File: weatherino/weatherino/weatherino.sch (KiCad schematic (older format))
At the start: 11 parts, among them U1 TP4056_BD, U2 BMP280_BD, U3 SHT31_BD, U4 Moteino_hcw

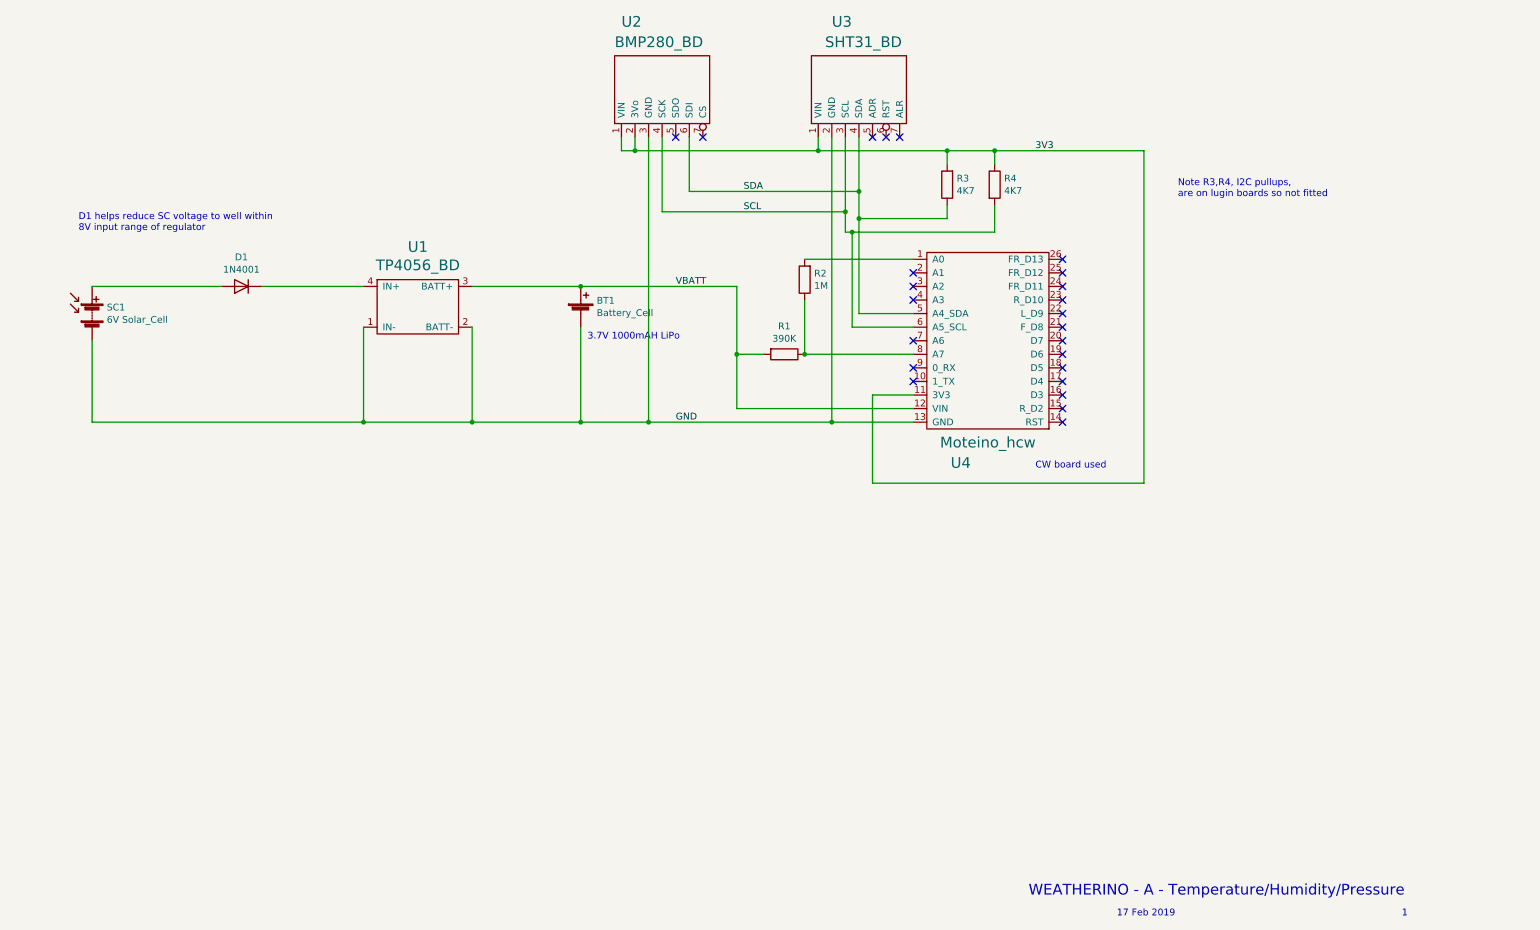
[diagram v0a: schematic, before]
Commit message: update schematic
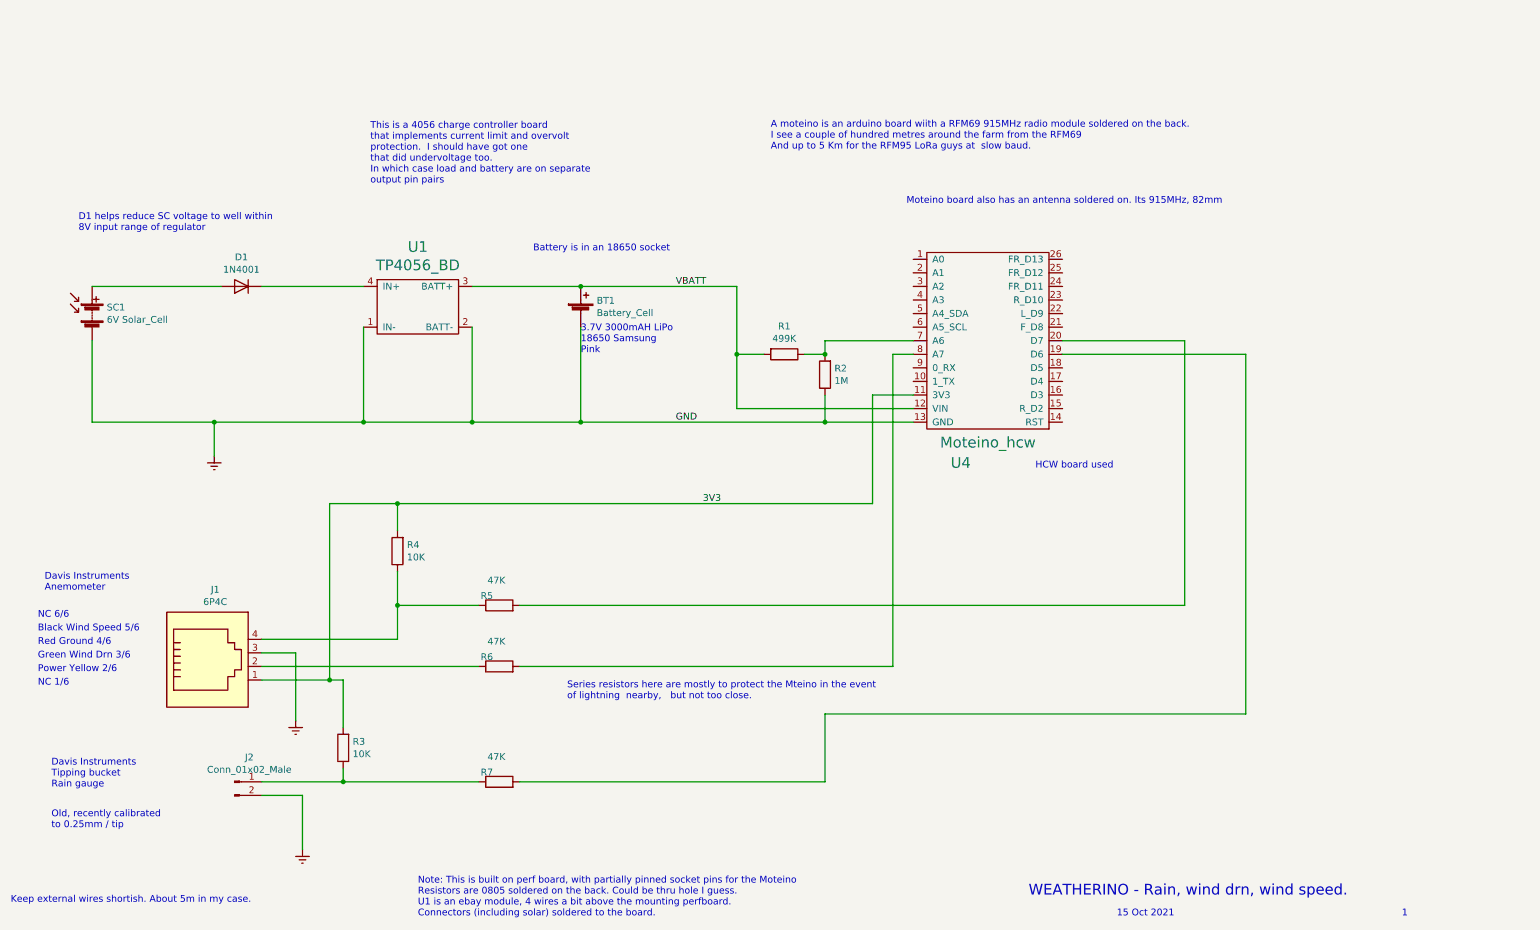
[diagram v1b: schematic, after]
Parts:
- removed U2: BMP280_BD, symbol swinggate_sch:BMP280_BD
- removed U3: SHT31_BD, symbol swinggate_sch:SHT31_BD
- added J1: 6P4C, symbol Connector:6P4C
- added J2: Conn_01x02_Male, symbol Connector:Conn_01x02_Male
- added R4: 10K, symbol Device:R
- added R5, R7: 47K, symbol Device:R
- R1: value 390K -> 499K
- R3: value 4K7 -> 10K
- R6: renamed from R4; value 4K7 -> 47K
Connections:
- net 3V3: now also J1.1, R4.2; no longer R6.1
- net at U4.1 (A0): no longer R2.2
- net at U4.19 (D6): now also R7.2
- net at U4.20 (D7): now also R5.2
- net at U4.7 (A6): now also R1.1, R2.2
- net GND renamed Earth
- net Earth: now also R2.1, J1.3, J2.2 (Pin_2)
- net SCL: no longer names the net of U4.6 (A5_SCL)
- net SCL: no longer R6.2
- net SDA: no longer names the net of U4.5 (A4_SDA)
- net SDA: no longer R3.1
- new net: R6.2, U4.8 (A7)
- new net: J1.2, R6.1
- new net: J2.1 (Pin_1), R3.1, R7.1
- new net: J1.4, R4.1, R5.1
- no-connect marks 24 -> 0
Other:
- note added: "15 Oct 2021"
- note added: "3.7V 3000mAH LiPo \n18650 Samsung\nPink"
- note added: "A moteino is an arduino board wiith a RFM69 915MHz radio module soldered on the back. \nI see a couple of hundred metres around the farm from the RFM69\nAnd up to 5 Km for the RFM95 LoRa guys at slow baud."
- note added: "Battery is in an 18650 socket"
- note added: "Black Wind Speed 5/6"
- note added: "Davis Instruments \nTipping bucket\nRain gauge"
- note added: "Davis Instruments\nAnemometer"
- note added: "Green Wind Drn 3/6"
- note added: "HCW board used"
- note added: "Keep external wires shortish. About 5m in my case."
- note added: "Moteino board also has an antenna soldered on. Its 915MHz, 82mm"
- note added: "NC 1/6"
- note added: "NC 6/6"
- note added: "Note: This is built on perf board, with partially pinned socket pins for the Moteino\nResistors are 0805 soldered on the back. Could be thru hole I guess.\nU1 is an ebay module, 4 wires a bit above the mounting perfboard.\nConnectors (including solar) soldered to the board."
- note added: "Old, recently calibrated\nto 0.25mm / tip"
- note added: "Power Yellow 2/6"
- note added: "Red Ground 4/6"
- note added: "Series resistors here are mostly to protect the Mteino in the event \nof lightning nearby, but not too close."
- note added: "This is a 4056 charge controller board\nthat implements current limit and overvolt \nprotection. I should have got one \nthat did undervoltage too. \nIn which case load and battery are on separate \noutput pin pairs"
- note added: "WEATHERINO - Rain, wind drn, wind speed."
- note removed: "17 Feb 2019"
- note removed: "3.7V 1000mAH LiPo"
- note removed: "CW board used"
- note removed: "Note R3,R4, I2C pullups,\nare on lugin boards so not fitted"
- note removed: "WEATHERINO - A - Temperature/Humidity/Pressure"
- moved on the sheet: R2, R6

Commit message: address emi susceptibility and contact bounce on rain.
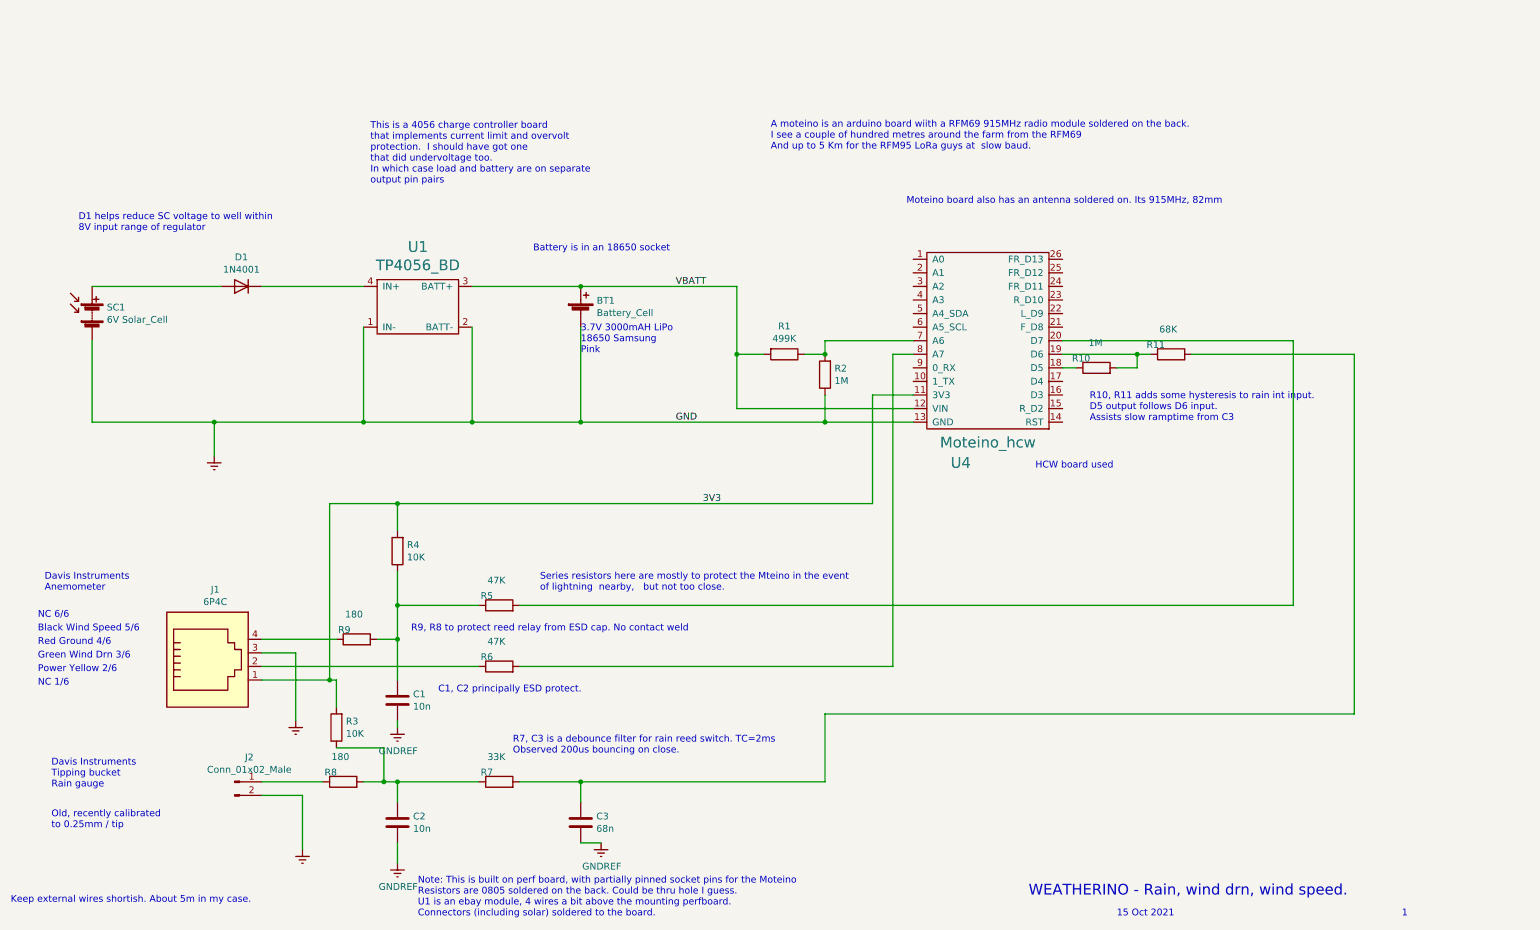
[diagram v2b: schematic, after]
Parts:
- added C1, C2: 10n, symbol Device:C
- added C3: 68n, symbol Device:C
- added R10: 1M, symbol Device:R
- added R11: 68K, symbol Device:R
- added R8, R9: 180, symbol Device:R
- R7: value 47K -> 33K
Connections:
- net at U4.18 (D5): now also R10.1
- net at U4.19 (D6): now also R10.2, R11.1; no longer R7.2
- net at R3.1, R7.1: now also C2.1, R8.2; no longer J2.1 (Pin_1)
- net at R4.1, R5.1: now also C1.1, R9.2; no longer J1.4
- new net: J2.1 (Pin_1), R8.1
- new net: J1.4, R9.1
- new net: C3.1, R11.2, R7.2
- new net GNDREF: C1.2, C2.2, C3.2
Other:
- note added: "C1, C2 principally ESD protect."
- note added: "R10, R11 adds some hysteresis to rain int input. \nD5 output follows D6 input. \nAssists slow ramptime from C3"
- note added: "R7, C3 is a debounce filter for rain reed switch. TC=2ms\nObserved 200us bouncing on close."
- note added: "R9, R8 to protect reed relay from ESD cap. No contact weld"
- moved on the sheet: R3
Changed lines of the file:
@@
 L Device:R R3
 U 1 1 616CDA02
-P 2950 6400
-F 0 "R3" H 2880 6354 50  0000 R CNN
-F 1 "10K" H 2880 6445 50  0000 R CNN
-F 2 "" V 2880 6400 50  0001 C CNN
-F 3 "~" H 2950 6400 50  0001 C CNN
-	1    2950 6400
+P 2900 6250
+F 0 "R3" H 2830 6204 50  0000 R CNN
+F 1 "10K" H 2830 6295 50  0000 R CNN
+F 2 "" V 2830 6250 50  0001 C CNN
+F 3 "~" H 2900 6250 50  0001 C CNN
+	1    2900 6250
 	-1   0    0    1
 $EndComp
-Wire Wire Line
-	2950 6550 2950 6650
 $Comp
 L Device:R R7
@@
 P 4100 6650
 F 0 "R7" V 4170 6696 50  0000 L CNN
-F 1 "47K" V 4284 6605 50  0000 L CNN
+F 1 "33K" V 4284 6605 50  0000 L CNN
 F 2 "" V 4030 6650 50  0001 C CNN
 F 3 "~" H 4100 6650 50  0001 C CNN
@@
 $EndComp
 Wire Wire Line
-	2950 6250 2950 5900
-Wire Wire Line
-	2950 5900 2850 5900
-Connection ~ 2850 5900
-Wire Wire Line
 	3350 4800 3350 4600
 Connection ~ 3350 4600
@@
 	3350 5100 3350 5350
 Wire Wire Line
-	2350 5600 3350 5600
-Wire Wire Line
 	3350 5600 3350 5350
 Connection ~ 3350 5350
 Wire Wire Line
 	2350 5800 3950 5800
-Wire Wire Line
-	2350 6650 2950 6650
-Wire Wire Line
-	2950 6650 3950 6650
-Connection ~ 2950 6650
 Wire Wire Line
 	6850 3800 6850 4600
@@
 $EndComp
 Wire Wire Line
-	4250 5350 9150 5350
-Wire Wire Line
 	7150 3400 6500 3400
 Wire Wire Line
@@
 	6500 6650 6500 6150
 Wire Wire Line
-	6500 6150 9600 6150
-Wire Wire Line
-	9600 6150 9600 3500
-Wire Wire Line
-	4250 6650 6500 6650
-Wire Wire Line
-	8250 3500 9600 3500
-Wire Wire Line
-	8250 3400 9150 3400
-Wire Wire Line
-	9150 3400 9150 5350
+	10400 6150 10400 3500
+Wire Wire Line
+	4250 6650 4700 6650
+Wire Wire Line
+	9950 3400 9950 5350
 Wire Wire Line
 	7000 3500 7000 5800
@@
 Text Notes 3500 7650 0    50   ~ 0
 Note: This is built on perf board, with partially pinned socket pins for the Moteino\nResistors are 0805 soldered on the back. Could be thru hole I guess.\nU1 is an ebay module, 4 wires a bit above the mounting perfboard.\nConnectors (including solar) soldered to the board.
-Text Notes 4600 6050 0    50   ~ 0
+Text Notes 4400 5250 0    50   ~ 0
 Series resistors here are mostly to protect the Mteino in the event \nof lightning  nearby,   but not too close.
 Text Notes 500  7550 0    50   ~ 0
@@
 Text Notes 6100 2000 0    50   ~ 0
 A moteino is an arduino board wiith a RFM69 915MHz radio module soldered on the back.  \nI see a couple of hundred metres around the farm from the RFM69\nAnd up to 5 Km for the RFM95 LoRa guys at  slow baud.
+$Comp
+L Device:R R10
+U 1 1 6175B278
+P 8500 3600
+F 0 "R10" V 8570 3646 50  0000 L CNN
+F 1 "1M" V 8684 3555 50  0000 L CNN
+F 2 "" V 8430 3600 50  0001 C CNN
+F 3 "~" H 8500 3600 50  0001 C CNN
+	1    8500 3600
+	0    -1   -1   0
+$EndComp
+$Comp
+L Device:R R11
+U 1 1 6175C380
+P 9050 3500
+F 0 "R11" V 9120 3546 50  0000 L CNN
+F 1 "68K" V 9234 3455 50  0000 L CNN
+F 2 "" V 8980 3500 50  0001 C CNN
+F 3 "~" H 9050 3500 50  0001 C CNN
+	1    9050 3500
+	0    -1   -1   0
+$EndComp
+Wire Wire Line
+	8250 3600 8350 3600
+Wire Wire Line
+	8250 3500 8800 3500
+Wire Wire Line
+	8650 3600 8800 3600
+Wire Wire Line
+	8800 3600 8800 3500
+Connection ~ 8800 3500
+Wire Wire Line
+	8800 3500 8900 3500
+Wire Wire Line
+	8250 3400 9950 3400
+Wire Wire Line
+	4250 5350 9950 5350
+Wire Wire Line
+	9200 3500 10400 3500
+Wire Wire Line
+	6500 6150 10400 6150
+$Comp
+L Device:R R8
+U 1 1 61783C0D
+P 2950 6650
+F 0 "R8" V 3020 6696 50  0000 L CNN
+F 1 "180" V 3134 6605 50  0000 L CNN
+F 2 "" V 2880 6650 50  0001 C CNN
+F 3 "~" H 2950 6650 50  0001 C CNN
+	1    2950 6650
+	0    -1   -1   0
+$EndComp
+$Comp
+L Device:C C2
+U 1 1 61785064
+P 3350 6950
+F 0 "C2" H 3465 6996 50  0000 L CNN
+F 1 "10n" H 3465 6905 50  0000 L CNN
+F 2 "" H 3388 6800 50  0001 C CNN
+F 3 "~" H 3350 6950 50  0001 C CNN
+	1    3350 6950
+	1    0    0    -1
+$EndComp
+$Comp
+L Device:C C3
+U 1 1 61785E2B
+P 4700 6950
+F 0 "C3" H 4815 6996 50  0000 L CNN
+F 1 "68n" H 4815 6905 50  0000 L CNN
+F 2 "" H 4738 6800 50  0001 C CNN
+F 3 "~" H 4700 6950 50  0001 C CNN
+	1    4700 6950
+	1    0    0    -1
+$EndComp
+$Comp
+L Device:C C1
+U 1 1 6178DBD0
+P 3350 6050
+F 0 "C1" H 3465 6096 50  0000 L CNN
+F 1 "10n" H 3465 6005 50  0000 L CNN
+F 2 "" H 3388 5900 50  0001 C CNN
+F 3 "~" H 3350 6050 50  0001 C CNN
+	1    3350 6050
+	1    0    0    -1
+$EndComp
+$Comp
+L Device:R R9
+U 1 1 6178FA99
+P 3050 5600
+F 0 "R9" V 3120 5646 50  0000 L CNN
+F 1 "180" V 3234 5555 50  0000 L CNN
+F 2 "" V 2980 5600 50  0001 C CNN
+F 3 "~" H 3050 5600 50  0001 C CNN
+	1    3050 5600
+	0    -1   -1   0
+$EndComp
+$Comp
+L power:GNDREF #PWR02
+U 1 1 617934F1
+P 3350 7250
+F 0 "#PWR02" H 3350 7000 50  0001 C CNN
+F 1 "GNDREF" H 3355 7077 50  0000 C CNN
+F 2 "" H 3350 7250 50  0001 C CNN
+F 3 "" H 3350 7250 50  0001 C CNN
+	1    3350 7250
+	1    0    0    -1
+$EndComp
+$Comp
+L power:GNDREF #PWR03
+U 1 1 617940BA
+P 4850 7100
+F 0 "#PWR03" H 4850 6850 50  0001 C CNN
+F 1 "GNDREF" H 4855 6927 50  0000 C CNN
+F 2 "" H 4850 7100 50  0001 C CNN
+F 3 "" H 4850 7100 50  0001 C CNN
+	1    4850 7100
+	1    0    0    -1
+$EndComp
+$Comp
+L power:GNDREF #PWR01
+U 1 1 61794C63
+P 3350 6250
+F 0 "#PWR01" H 3350 6000 50  0001 C CNN
+F 1 "GNDREF" H 3355 6077 50  0000 C CNN
+F 2 "" H 3350 6250 50  0001 C CNN
+F 3 "" H 3350 6250 50  0001 C CNN
+	1    3350 6250
+	1    0    0    -1
+$EndComp
+Wire Wire Line
+	2350 5600 2900 5600
+Wire Wire Line
+	3200 5600 3350 5600
+Wire Wire Line
+	3350 5900 3350 5600
+Connection ~ 3350 5600
+Wire Wire Line
+	3350 6250 3350 6200
+Wire Wire Line
+	2350 6650 2800 6650
+Wire Wire Line
+	3100 6650 3250 6650
+Wire Wire Line
+	3350 6800 3350 6650
+Connection ~ 3350 6650
+Wire Wire Line
+	3350 6650 3950 6650
+Wire Wire Line
+	3350 7250 3350 7100
+Wire Wire Line
+	4700 7100 4850 7100
+Wire Wire Line
+	4700 6800 4700 6650
+Connection ~ 4700 6650
+Wire Wire Line
+	4700 6650 6500 6650
+Wire Wire Line
+	2900 6400 3250 6400
+Wire Wire Line
+	3250 6400 3250 6650
+Connection ~ 3250 6650
+Wire Wire Line
+	3250 6650 3350 6650
+Wire Wire Line
+	2900 6100 2900 5900
+Wire Wire Line
+	2900 5900 2850 5900
+Connection ~ 2850 5900
+Text Notes 3650 6000 0    50   ~ 0
+C1, C2 principally ESD protect.
+Text Notes 3450 5550 0    50   ~ 0
+R9, R8 to protect reed relay from ESD cap. No contact weld
+Text Notes 4200 6450 0    50   ~ 0
+R7, C3 is a debounce filter for rain reed switch. TC=2ms\nObserved 200us bouncing on close.
+Text Notes 8450 4000 0    50   ~ 0
+R10, R11 adds some hysteresis to rain int input. \nD5 output follows D6 input. \nAssists slow ramptime from C3
 $EndSCHEMATC
